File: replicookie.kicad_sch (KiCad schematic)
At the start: 0 parts

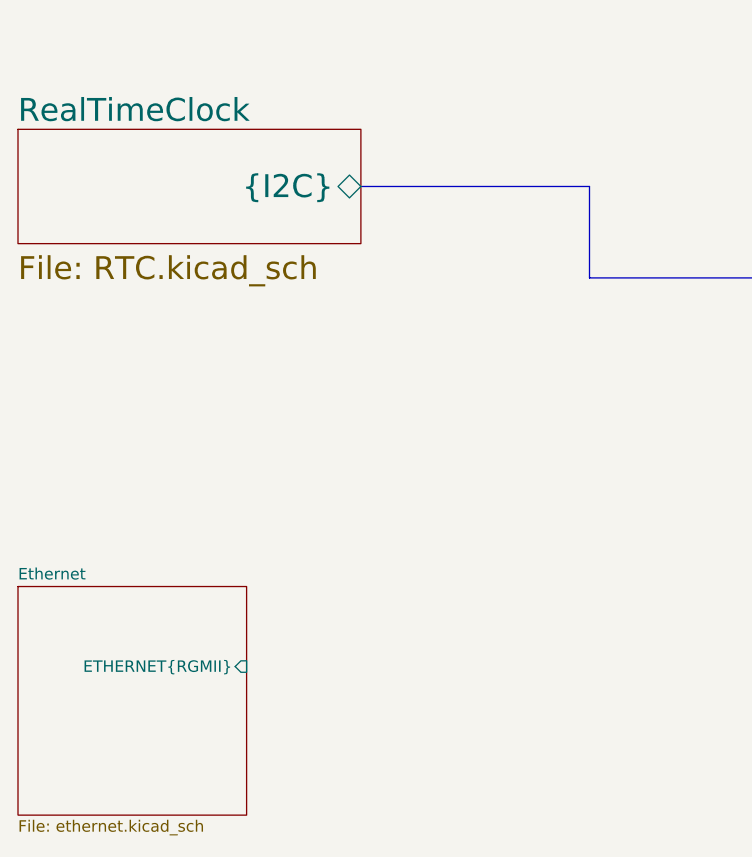
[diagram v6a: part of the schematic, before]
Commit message: Add ULPI USB PHY
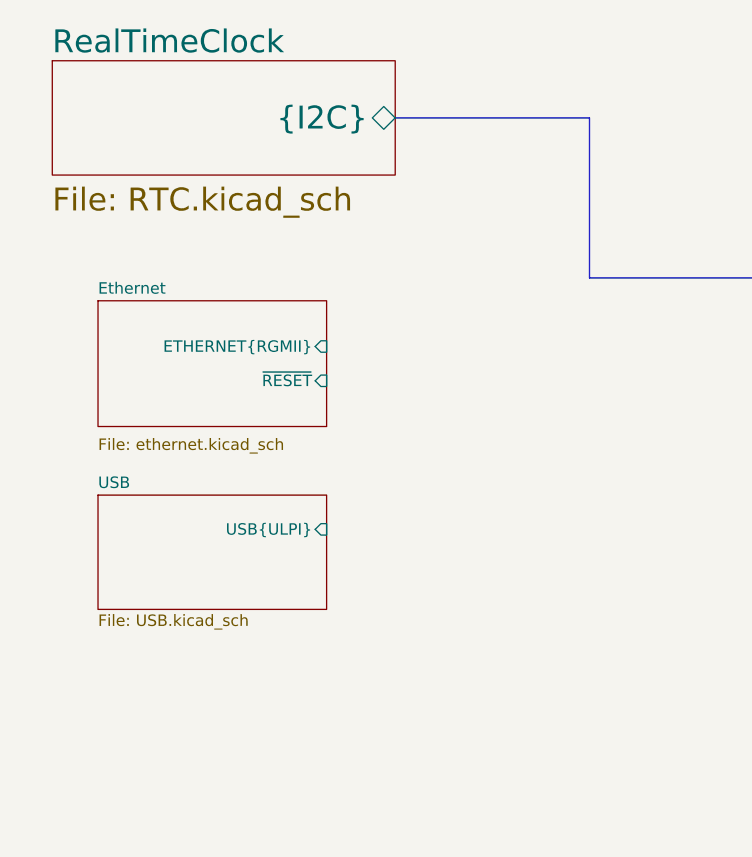
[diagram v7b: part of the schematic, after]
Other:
- added sheet USB (USB.kicad_sch)
- sheet Ethernet ports: added ~RESET; removed none
- company: Drawn by: Cameron McQuinn -> (none)
- title: Snickerdoodle Baseboard -> Replicookie
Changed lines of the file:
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@@
 (kicad_sch (version 20200618) (host eeschema "5.99.0-unknown-77313e4~101~ubuntu20.04.1")
-  (page 1 13)
+  (page 1 14)
   (paper "B")
   (title_block
-    (title "Snickerdoodle Baseboard")
+    (title "Replicookie")
     (date "2020-06-24")
     (rev "1.0")
-    (company "Drawn by: Cameron McQuinn")
     (comment 1 "Drawn by: Cameron McQuinn")
   )
-  (bus (pts (xy 101.6 69.85) (xy 127 69.85))
+  (bus (pts (xy 105.41 62.23) (xy 127 62.23))
     (stroke (width 0) (type solid) (color 0 0 0 0))
   )
-  (bus (pts (xy 127 69.85) (xy 127 80.01))
+  (bus (pts (xy 127 62.23) (xy 127 80.01))
     (stroke (width 0) (type solid) (color 0 0 0 0))
   )
@@
     (stroke (width 0) (type solid) (color 0 0 0 0))
   )
-  (sheet (at 63.5 114.3) (size 25.4 25.4)
+  (sheet (at 72.39 82.55) (size 25.4 13.97)
     (stroke (width 0.0006) (type solid) (color 132 0 132 1))
     (fill (color 255 255 255 0.0000))
-    (property "Sheet name" "Ethernet" (id 0) (at 63.5 113.6643 0)
+    (property "Sheet name" "Ethernet" (id 0) (at 72.39 81.9143 0)
       (effects (font (size 1.27 1.27)) (justify left bottom))
     )
-    (property "Sheet file" "ethernet.kicad_sch" (id 1) (at 63.5 140.2087 0)
+    (property "Sheet file" "ethernet.kicad_sch" (id 1) (at 72.39 97.79 0)
       (effects (font (size 1.27 1.27)) (justify left top))
     )
-    (pin "ETHERNET{RGMII}" input (at 88.9 123.19 0)
+    (pin "ETHERNET{RGMII}" input (at 97.79 87.63 0)
+      (effects (font (size 1.27 1.27)) (justify right))
+    )
+    (pin "~RESET" input (at 97.79 91.44 0)
       (effects (font (size 1.27 1.27)) (justify right))
     )
@@
     )
   )
-  (sheet (at 63.5 63.5) (size 38.1 12.7)
+  (sheet (at 67.31 55.88) (size 38.1 12.7)
     (stroke (width 0.0006) (type solid) (color 132 0 132 1))
     (fill (color 255 255 255 0.0000))
-    (property "Sheet name" "RealTimeClock" (id 0) (at 63.5 62.8643 0)
+    (property "Sheet name" "RealTimeClock" (id 0) (at 67.31 55.2443 0)
       (effects (font (size 2.54 2.54)) (justify left bottom))
     )
-    (property "Sheet file" "RTC.kicad_sch" (id 1) (at 63.5 77.47 0)
+    (property "Sheet file" "RTC.kicad_sch" (id 1) (at 67.31 69.85 0)
       (effects (font (size 2.54 2.54)) (justify left top))
     )
-    (pin "{I2C}" bidirectional (at 101.6 69.85 0)
+    (pin "{I2C}" bidirectional (at 105.41 62.23 0)
       (effects (font (size 2.54 2.54)) (justify right))
     )
@@
     )
   )
+  (sheet (at 72.39 104.14) (size 25.4 12.7)
+    (stroke (width 0.0006) (type solid) (color 132 0 132 1))
+    (fill (color 255 255 255 0.0000))
+    (property "Sheet name" "USB" (id 0) (at 72.39 103.5043 0)
+      (effects (font (size 1.27 1.27)) (justify left bottom))
+    )
+    (property "Sheet file" "USB.kicad_sch" (id 1) (at 72.39 117.3487 0)
+      (effects (font (size 1.27 1.27)) (justify left top))
+    )
+    (pin "USB{ULPI}" input (at 97.79 107.95 0)
+      (effects (font (size 1.27 1.27)) (justify right))
+    )
+  )
   (symbol_instances
     (path "/655846c9-6d11-4b61-aecf-3ea94510aa57/a31059e0-2106-4ba5-9ab1-2330ed94e840"
@@
       (reference "#PWR0331") (unit 1)
     )
+    (path "/0f4efdfd-e05f-4498-9f56-5655a2aa694e/cc2ce420-7535-4224-9f53-5d81b2e77819"
+      (reference "#PWR0332") (unit 1)
+    )
     (path "/0f4efdfd-e05f-4498-9f56-5655a2aa694e/a41a30a7-3c00-4db9-945e-ded3cec11ac6"
       (reference "C301") (unit 1)
@@
       (reference "C328") (unit 1)
     )
-    (path "/0f4efdfd-e05f-4498-9f56-5655a2aa694e/7b1a44ba-1680-4634-a561-975ef8a568bf"
+    (path "/0f4efdfd-e05f-4498-9f56-5655a2aa694e/c3dcb01b-40bc-469a-a3ad-e1dafcdc97bf"
       (reference "D301") (unit 1)
     )
-    (path "/0f4efdfd-e05f-4498-9f56-5655a2aa694e/066f67a6-2acb-4729-aa95-77345fa36f36"
+    (path "/0f4efdfd-e05f-4498-9f56-5655a2aa694e/7b9c1687-7630-4bd6-b3a9-31d14d5b39ec"
       (reference "D302") (unit 1)
     )
@@
       (reference "X301") (unit 1)
     )
+    (path "/5305719f-293c-4859-8d79-7c90ef688f80/40c22255-a29b-483b-a8d9-6f5cd62e9c99"
+      (reference "#PWR0416") (unit 1)
+    )
+    (path "/5305719f-293c-4859-8d79-7c90ef688f80/a3dc2c13-e212-4716-83d3-270c88374b15"
+      (reference "#PWR0417") (unit 1)
+    )
+    (path "/5305719f-293c-4859-8d79-7c90ef688f80/5f678ffb-f0cd-4462-b52c-b25fd889c286"
+      (reference "#PWR0418") (unit 1)
+    )
+    (path "/5305719f-293c-4859-8d79-7c90ef688f80/b2c03226-09f1-489e-a1e8-c3aa424d7834"
+      (reference "#PWR0419") (unit 1)
+    )
+    (path "/5305719f-293c-4859-8d79-7c90ef688f80/43344dad-baa7-4d17-9950-73be152d0a52"
+      (reference "#PWR0420") (unit 1)
+    )
+    (path "/5305719f-293c-4859-8d79-7c90ef688f80/101485aa-4b3e-4545-827b-4e9f9033f054"
+      (reference "#PWR0421") (unit 1)
+    )
+    (path "/5305719f-293c-4859-8d79-7c90ef688f80/336db8c8-dcb6-4902-b86c-8e589b17812a"
+      (reference "#PWR0422") (unit 1)
+    )
+    (path "/5305719f-293c-4859-8d79-7c90ef688f80/19a8ee14-1da8-4ad6-90e8-d4746647b290"
+      (reference "#PWR0423") (unit 1)
+    )
+    (path "/5305719f-293c-4859-8d79-7c90ef688f80/666cb924-b6b3-4d29-a690-9f39bc70f790"
+      (reference "C401") (unit 1)
+    )
+    (path "/5305719f-293c-4859-8d79-7c90ef688f80/6e6ef244-425c-4e57-8fc4-9b1901676610"
+      (reference "C402") (unit 1)
+    )
+    (path "/5305719f-293c-4859-8d79-7c90ef688f80/371d575f-6782-4c52-ac9f-a33c79a38cf3"
+      (reference "C403") (unit 1)
+    )
+    (path "/5305719f-293c-4859-8d79-7c90ef688f80/578cf62d-88d0-4cc5-9df7-a4a5fc71a658"
+      (reference "C404") (unit 1)
+    )
+    (path "/5305719f-293c-4859-8d79-7c90ef688f80/8ca313a0-161a-4029-8ba9-8ab382560567"
+      (reference "C405") (unit 1)
+    )
+    (path "/5305719f-293c-4859-8d79-7c90ef688f80/202429c4-8088-40ab-b092-d8b07b346b78"
+      (reference "C406") (unit 1)
+    )
+    (path "/5305719f-293c-4859-8d79-7c90ef688f80/c9ead347-2847-438d-92b2-370130e7556c"
+      (reference "R401") (unit 1)
+    )
+    (path "/5305719f-293c-4859-8d79-7c90ef688f80/fee2918f-c5a5-4c16-9140-d1198bfe33bc"
+      (reference "R402") (unit 1)
+    )
+    (path "/5305719f-293c-4859-8d79-7c90ef688f80/9718e817-7e5e-487b-8f6b-fc1b3c42636e"
+      (reference "U401") (unit 1)
+    )
+    (path "/5305719f-293c-4859-8d79-7c90ef688f80/500f21ab-f388-4c86-90c0-2a9ff801fa06"
+      (reference "U402") (unit 1)
+    )
     (path "/a32a7713-aceb-431f-82b6-7899cc3ddd29/98a5fdfe-900b-4e5e-a7b9-3aae14bcaa54"
